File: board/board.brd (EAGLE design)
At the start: 94 x 44.5 mm, 68 parts, among them Q2 ULN2003AD

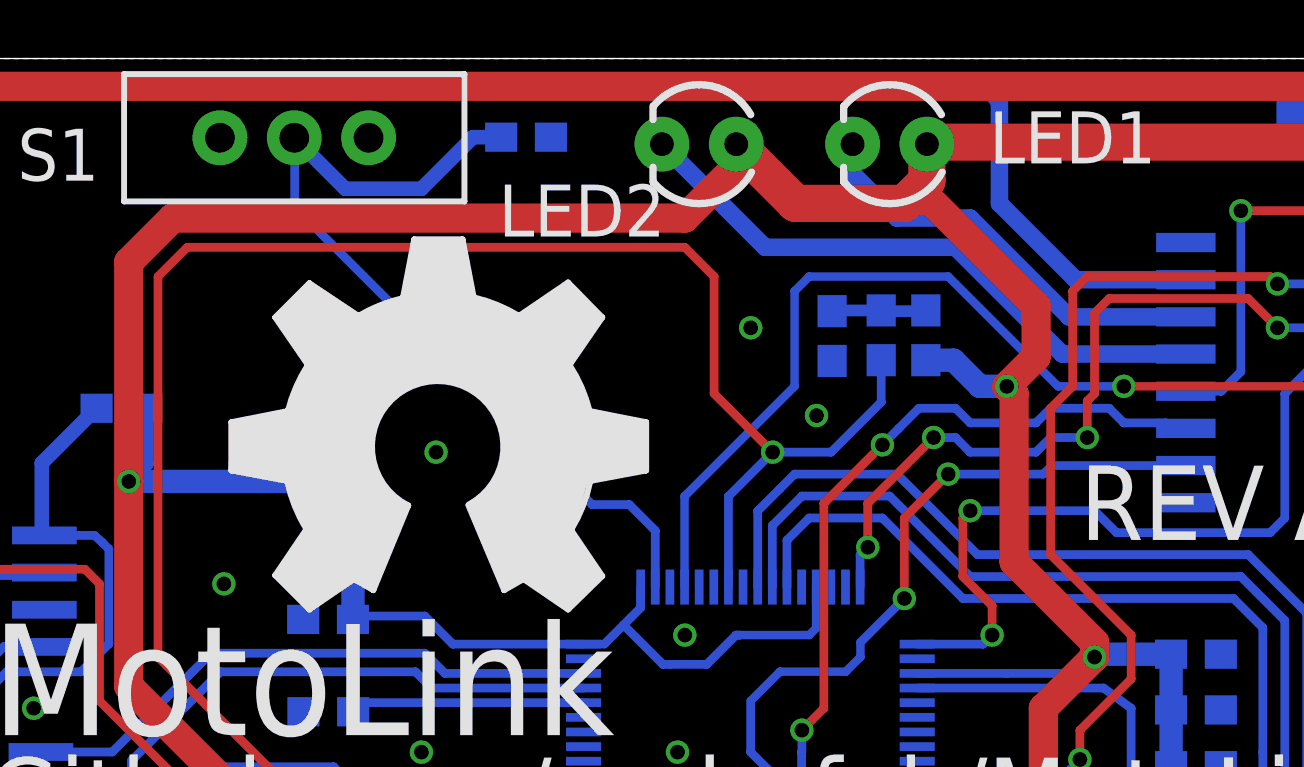
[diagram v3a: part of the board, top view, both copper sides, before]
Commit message: Adding HSE Crystal, needed for USB.
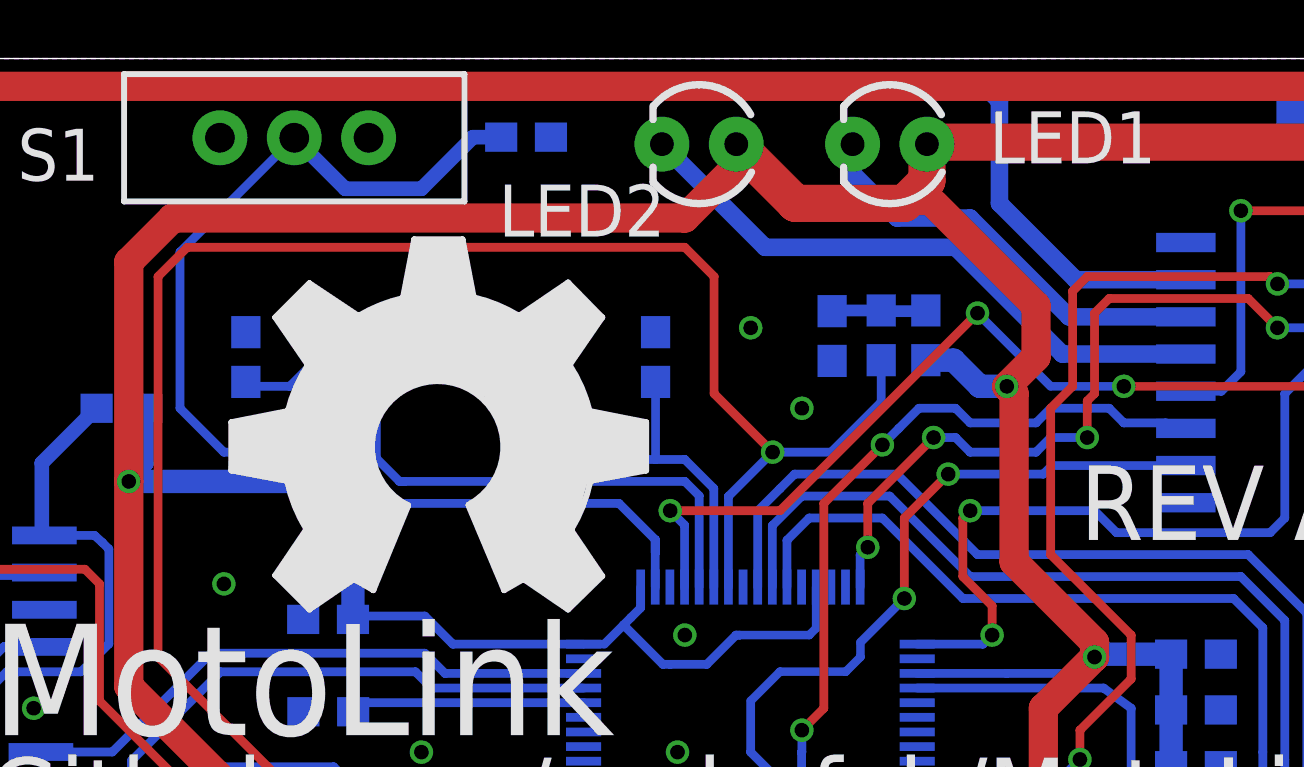
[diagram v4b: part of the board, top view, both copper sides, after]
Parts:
- added C5, C7: 4.7pF, SparkFun-Capacitors:0603-CAP
- added Y1: (no value), SparkFun-FreqCtrl:HC49US
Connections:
- new net OSC_IN: C5.2, STM32.6, Y1.1
- new net OSC_OUT: C7.2, STM32.5, Y1.2
- net GND: now also C5.1, C7.1
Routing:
- net OSC_OUT: track 0.00 -> 23.0 mm
- net OSC_IN: track 0.00 -> 16.0 mm
- net BUT1: track 29.7 -> 40.0 mm
- net USB_VBUS_CTRL: track 39.6 -> 37.1 mm, vias 2 -> 4
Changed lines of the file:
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@@
 <layer number="19" name="Unrouted" color="6" fill="1" visible="yes" active="yes"/>
 <layer number="20" name="Dimension" color="15" fill="1" visible="yes" active="yes"/>
-<layer number="21" name="tPlace" color="16" fill="1" visible="yes" active="yes"/>
+<layer number="21" name="tPlace" color="16" fill="1" visible="no" active="yes"/>
 <layer number="22" name="bPlace" color="14" fill="1" visible="yes" active="yes"/>
 <layer number="23" name="tOrigins" color="15" fill="1" visible="yes" active="yes"/>
@@
 <attribute name="VALUE" x="3.901" y="20.754" size="0.4064" layer="28" rot="MR90"/>
 </element>
+<element name="Y1" library="SparkFun-FreqCtrl" package="HC49US" value="" x="32" y="34.25" smashed="yes" rot="MR0">
+<attribute name="NAME" x="33.465" y="29.794" size="1.778" layer="26" font="vector" ratio="16" rot="MR0"/>
+<attribute name="VALUE" x="37.715" y="30.059" size="1.27" layer="28" ratio="10" rot="MR0"/>
+</element>
+<element name="C5" library="SparkFun-Capacitors" package="0603-CAP" value="4.7pF" x="39" y="34.25" smashed="yes" rot="MR270">
+<attribute name="NAME" x="40.389" y="30.762" size="1.778" layer="26" font="vector" ratio="16" rot="MR0"/>
+<attribute name="VALUE" x="40.143" y="35.266" size="0.4064" layer="28" font="vector" rot="MR270"/>
+</element>
+<element name="C7" library="SparkFun-Capacitors" package="0603-CAP" value="4.7pF" x="25" y="34.25" smashed="yes" rot="MR270">
+<attribute name="NAME" x="23.111" y="32.488" size="1.778" layer="26" font="vector" ratio="16" rot="MR180"/>
+<attribute name="VALUE" x="26.143" y="35.266" size="0.4064" layer="28" font="vector" rot="MR270"/>
+</element>
 </elements>
 <signals>
@@
 <via x="81" y="3" extent="1-16" drill="0.5"/>
 <via x="88.5" y="32" extent="1-16" drill="0.5"/>
-<via x="31.5" y="31" extent="1-16" drill="0.5"/>
+<via x="32" y="34.25" extent="1-16" drill="0.5"/>
 <via x="65.5" y="24" extent="1-16" drill="0.5"/>
 <via x="2.25" y="20.5" extent="1-16" drill="0.5"/>
@@
 <via x="17.75" y="22.25" extent="1-16" drill="0.5"/>
 <contactref element="CON_KNK" pad="1"/>
-<via x="44.5" y="32.25" extent="1-16" drill="0.5"/>
+<via x="44" y="32.5" extent="1-16" drill="0.5"/>
 <via x="49.25" y="4" extent="1-16" drill="0.5"/>
 <via x="72.25" y="21.5" extent="1-16" drill="0.5"/>
@@
 <contactref element="TVS1" pad="A"/>
 <contactref element="IC_KLINE" pad="5"/>
+<contactref element="C7" pad="1"/>
+<contactref element="C5" pad="1"/>
 </signal>
 <signal name="+3V3">
@@
 <wire x1="31" y1="40" x2="28.3975" y2="40" width="0.5" layer="16"/>
 <wire x1="28.3975" y1="40" x2="26.655" y2="41.7425" width="0.5" layer="16"/>
-<wire x1="38.99" y1="26.39" x2="38.99" y2="28.32" width="0.3" layer="16"/>
-<wire x1="38.99" y1="28.32" x2="38.1" y2="29.21" width="0.3" layer="16"/>
-<wire x1="38.1" y1="29.21" x2="36.83" y2="29.21" width="0.3" layer="16"/>
-<wire x1="36.83" y1="29.21" x2="26.67" y2="39.37" width="0.3" layer="16"/>
-<wire x1="26.67" y1="39.37" x2="26.67" y2="41.7275" width="0.3" layer="16"/>
+<wire x1="38.99" y1="26.39" x2="38.99" y2="27.57" width="0.3" layer="16"/>
+<wire x1="38.99" y1="27.57" x2="38.99" y2="28.01" width="0.3" layer="16"/>
+<wire x1="38.99" y1="28.01" x2="38.99" y2="27.57" width="0.3" layer="16"/>
 <wire x1="26.67" y1="41.7275" x2="26.655" y2="41.7425" width="0.3" layer="16"/>
+<wire x1="38.99" y1="27.57" x2="38.99" y2="28.01" width="0.3" layer="16"/>
+<wire x1="38.99" y1="28.01" x2="37.75" y2="29.25" width="0.3" layer="16"/>
+<wire x1="37.75" y1="29.25" x2="30" y2="29.25" width="0.3" layer="16"/>
+<wire x1="30" y1="29.25" x2="28.25" y2="31" width="0.3" layer="16"/>
+<wire x1="28.25" y1="31" x2="24.25" y2="31" width="0.3" layer="16"/>
+<wire x1="24.25" y1="31" x2="22.75" y2="32.5" width="0.3" layer="16"/>
+<wire x1="22.75" y1="32.5" x2="22.75" y2="37.8375" width="0.3" layer="16"/>
+<wire x1="22.75" y1="37.8375" x2="26.655" y2="41.7425" width="0.3" layer="16"/>
 </signal>
 <signal name="AN1">
@@
 <contactref element="Q2" pad="5"/>
 <contactref element="STM32" pad="4"/>
-<wire x1="39.99" y1="26.39" x2="39.99" y2="29.49" width="0.29" layer="16"/>
-<wire x1="39.99" y1="29.49" x2="43.75" y2="33.25" width="0.29" layer="16"/>
-<wire x1="52.75" y1="33.25" x2="55" y2="33.25" width="0.29" layer="16"/>
+<wire x1="52.5" y1="33.25" x2="55" y2="33.25" width="0.29" layer="16"/>
 <via x="55" y="33.25" extent="1-16" drill="0.5"/>
 <wire x1="55" y1="33.25" x2="64.5" y2="33.25" width="0.29" layer="1"/>
@@
 <wire x1="65" y1="33" x2="62.8484" y2="33" width="0.29" layer="16"/>
 <wire x1="62.8484" y1="33" x2="63.2659" y2="33.0825" width="0.29" layer="16"/>
-<wire x1="43.75" y1="33.25" x2="43.75" y2="36.5" width="0.29" layer="16"/>
-<wire x1="43.75" y1="36.5" x2="44.25" y2="37" width="0.29" layer="16"/>
-<wire x1="44.25" y1="37" x2="49" y2="37" width="0.29" layer="16"/>
-<wire x1="49" y1="37" x2="52.75" y2="33.25" width="0.29" layer="16"/>
+<wire x1="39.99" y1="26.39" x2="39.99" y2="28.51" width="0.3" layer="16"/>
+<wire x1="39.99" y1="28.51" x2="39.5" y2="29" width="0.3" layer="16"/>
+<via x="39.5" y="29" extent="1-16" drill="0.5"/>
+<wire x1="39.5" y1="29" x2="43.25" y2="29" width="0.3" layer="1"/>
+<wire x1="52.5" y1="33.25" x2="50" y2="35.75" width="0.3" layer="16"/>
+<via x="50" y="35.75" extent="1-16" drill="0.5"/>
+<wire x1="50" y1="35.75" x2="43.25" y2="29" width="0.3" layer="1"/>
 </signal>
 <signal name="N$18">
@@
 <wire x1="5" y1="24.25" x2="8.65" y2="24.25" width="0.5" layer="16"/>
 </signal>
+<signal name="OSC_IN">
+<contactref element="STM32" pad="6"/>
+<contactref element="Y1" pad="1"/>
+<wire x1="40.99" y1="26.39" x2="40.99" y2="29.76" width="0.3" layer="16"/>
+<contactref element="C5" pad="2"/>
+<wire x1="40.99" y1="29.76" x2="40" y2="30.75" width="0.3" layer="16"/>
+<wire x1="40" y1="30.75" x2="39" y2="30.75" width="0.3" layer="16"/>
+<wire x1="39" y1="30.75" x2="35.25" y2="30.75" width="0.3" layer="16"/>
+<wire x1="35.25" y1="30.75" x2="34.75" y2="31.25" width="0.3" layer="16"/>
+<wire x1="34.75" y1="31.25" x2="34.75" y2="34.04" width="0.3" layer="16"/>
+<wire x1="34.75" y1="34.04" x2="34.54" y2="34.25" width="0.3" layer="16"/>
+<wire x1="39" y1="33.4" x2="39" y2="30.75" width="0.3" layer="16"/>
+</signal>
+<signal name="OSC_OUT">
+<contactref element="STM32" pad="5"/>
+<contactref element="Y1" pad="2"/>
+<wire x1="40.49" y1="26.39" x2="40.49" y2="29.51" width="0.3" layer="16"/>
+<wire x1="40.49" y1="29.51" x2="40" y2="30" width="0.3" layer="16"/>
+<wire x1="40" y1="30" x2="30.424" y2="30" width="0.3" layer="16"/>
+<wire x1="30.424" y1="30" x2="30.25" y2="30" width="0.3" layer="16"/>
+<wire x1="29.46" y1="34.25" x2="29.46" y2="30.79" width="0.3" layer="16"/>
+<wire x1="29.46" y1="30.79" x2="30.25" y2="30" width="0.3" layer="16"/>
+<contactref element="C7" pad="2"/>
+<wire x1="29.46" y1="34.25" x2="27.5" y2="34.25" width="0.3" layer="16"/>
+<wire x1="27.5" y1="34.25" x2="26.5" y2="33.25" width="0.3" layer="16"/>
+<wire x1="26.5" y1="33.25" x2="25.4" y2="33.25" width="0.3" layer="16"/>
+<wire x1="25.4" y1="33.25" x2="25" y2="33.4" width="0.3" layer="16"/>
+</signal>
 </signals>
